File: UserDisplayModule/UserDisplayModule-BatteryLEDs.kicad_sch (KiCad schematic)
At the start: 17 parts, among them U5 74HC595

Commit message: doubled LEDs + started PCB
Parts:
- removed D10: BAT3, symbol Device:LED
- removed D5: BAT8, symbol Device:LED
- removed D6: BAT7, symbol Device:LED
- removed D7: BAT6, symbol Device:LED
- removed D8: BAT5, symbol Device:LED
- removed D9: BAT4, symbol Device:LED
- added D13: BAT7, LED_SMD:LED_0805_2012Metric, symbol Device:LED
- added D14, D16, D18, D20, D22, D24, D25, D26: BAT1, LED_SMD:LED_0805_2012Metric, symbol Device:LED
- added D15: BAT6, LED_SMD:LED_0805_2012Metric, symbol Device:LED
- added D17: BAT5, LED_SMD:LED_0805_2012Metric, symbol Device:LED
- added D19: BAT4, LED_SMD:LED_0805_2012Metric, symbol Device:LED
- added D21: BAT3, LED_SMD:LED_0805_2012Metric, symbol Device:LED
- added D23: BAT2, LED_SMD:LED_0805_2012Metric, symbol Device:LED
- D11: value BAT2 -> BAT8; footprint (none) -> LED_SMD:LED_0805_2012Metric
- D12: footprint (none) -> LED_SMD:LED_0805_2012Metric
- R10, R11, R12, R5, R6, R7, R8, R9: footprint (none) -> Resistor_SMD:R_0805_2012Metric
- U5: footprint (none) -> ImportedFootprints:CD74HC595E
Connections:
- net GND: now also D14.1 (K), D16.1 (K), D18.1 (K), D20.1 (K), D22.1 (K), D24.1 (K), D26.1 (K); no longer D11.1 (K)
- net at R10.2: now also D21.2 (A)
- net at R6.2: now also D13.2 (A)
- net at R5.2: now also D11.2 (A)
- net at R7.2: now also D15.2 (A)
- net at R9.2: now also D19.2 (A)
- net at R8.2: now also D17.2 (A)
- net at D12.2 (A): now also D11.1 (K); no longer R12.2
- net at R11.2: now also D23.2 (A); no longer D11.2 (A)
- new net: D21.1 (K), D22.2 (A)
- new net: D13.1 (K), D14.2 (A)
- new net: D25.1 (K), D26.2 (A)
- new net: D19.1 (K), D20.2 (A)
- new net: D17.1 (K), D18.2 (A)
- new net: D23.1 (K), D24.2 (A)
- new net: D15.1 (K), D16.2 (A)
- new net: D25.2 (A), R12.2
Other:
- note added: "Battery Bar"

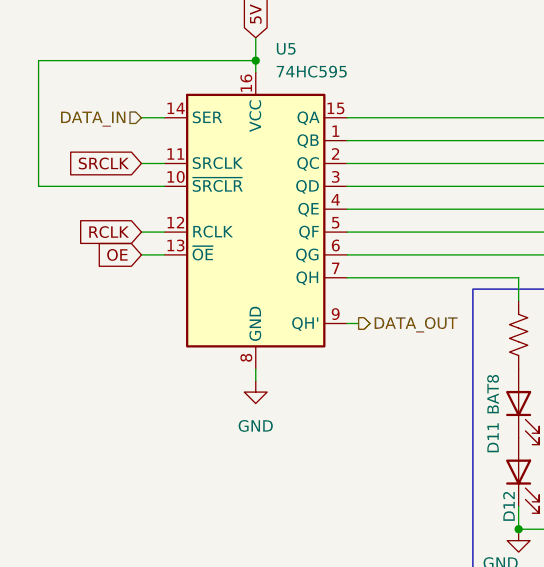
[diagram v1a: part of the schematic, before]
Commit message: finished routing pcb (minus ground pour)
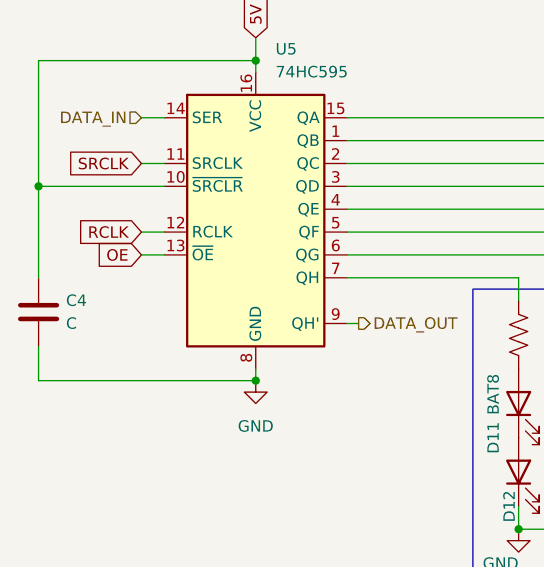
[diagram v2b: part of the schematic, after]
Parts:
- added C4: C, Capacitor_SMD:C_0805_2012Metric, symbol Device:C
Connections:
- net 5V: now also C4.1
- net GND: now also C4.2
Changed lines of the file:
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@@
+	)
+	(junction
+		(at 93.98 55.88)
+		(diameter 0)
+		(color 0 0 0 0)
 	)
 	(junction
@@
 		(color 0 0 0 0)
 	)
+	(junction
+		(at 118.11 77.47)
+		(diameter 0)
+		(color 0 0 0 0)
+	)
 	(wire
 		(pts
@@
 	(wire
 		(pts
+			(xy 93.98 77.47) (xy 118.11 77.47)
+		)
+		(stroke
+			(width 0)
+			(type default)
+		)
+	)
+	(wire
+		(pts
 			(xy 105.41 48.26) (xy 107.95 48.26)
 		)
@@
 	(wire
 		(pts
+			(xy 93.98 73.66) (xy 93.98 77.47)
+		)
+		(stroke
+			(width 0)
+			(type default)
+		)
+	)
+	(wire
+		(pts
 			(xy 175.26 93.98) (xy 189.23 93.98)
 		)
@@
 		(pts
 			(xy 217.17 93.98) (xy 231.14 93.98)
+		)
+		(stroke
+			(width 0)
+			(type default)
+		)
+	)
+	(wire
+		(pts
+			(xy 93.98 55.88) (xy 93.98 66.04)
 		)
 		(stroke
@@
 					(unit 1)
 				)
+			)
+		)
+	)
+	(symbol
+		(lib_id "Device:C")
+		(at 93.98 69.85 0)
+		(unit 1)
+		(exclude_from_sim no)
+		(in_bom yes)
+		(on_board yes)
+		(dnp no)
+		(property "Reference" "C4"
+			(at 97.028 68.58 0)
+			(effects
+				(font
+					(size 1.27 1.27)
+				)
+				(justify left)
+			)
+		)
+		(property "Value" "C"
+			(at 97.028 71.12 0)
+			(effects
+				(font
+					(size 1.27 1.27)
+				)
+				(justify left)
+			)
+		)
+		(property "Footprint" "Capacitor_SMD:C_0805_2012Metric"
+			(at 94.9452 73.66 0)
+			(effects
+				(font
+					(size 1.27 1.27)
+				)
+				(hide yes)
+			)
+		)
+		(property "Datasheet" "~"
+			(at 93.98 69.85 0)
+			(effects
+				(font
+					(size 1.27 1.27)
+				)
+				(hide yes)
+			)
+		)
+		(property "Description" "Unpolarized capacitor"
+			(at 93.98 69.85 0)
+			(effects
+				(font
+					(size 1.27 1.27)
+				)
+				(hide yes)
+			)
+		)
+		(pin "2"
+		)
+		(pin "1"
+		)
+		(instances
+			(project "UserDisplayModule"
+				(path "/352d7abe-fc72-4473-8b68-62eecf44f496/4dda0760-e028-41e6-8bb4-4ea7d454afd7"
+					(reference "C4")
+					(unit 1)
+				)

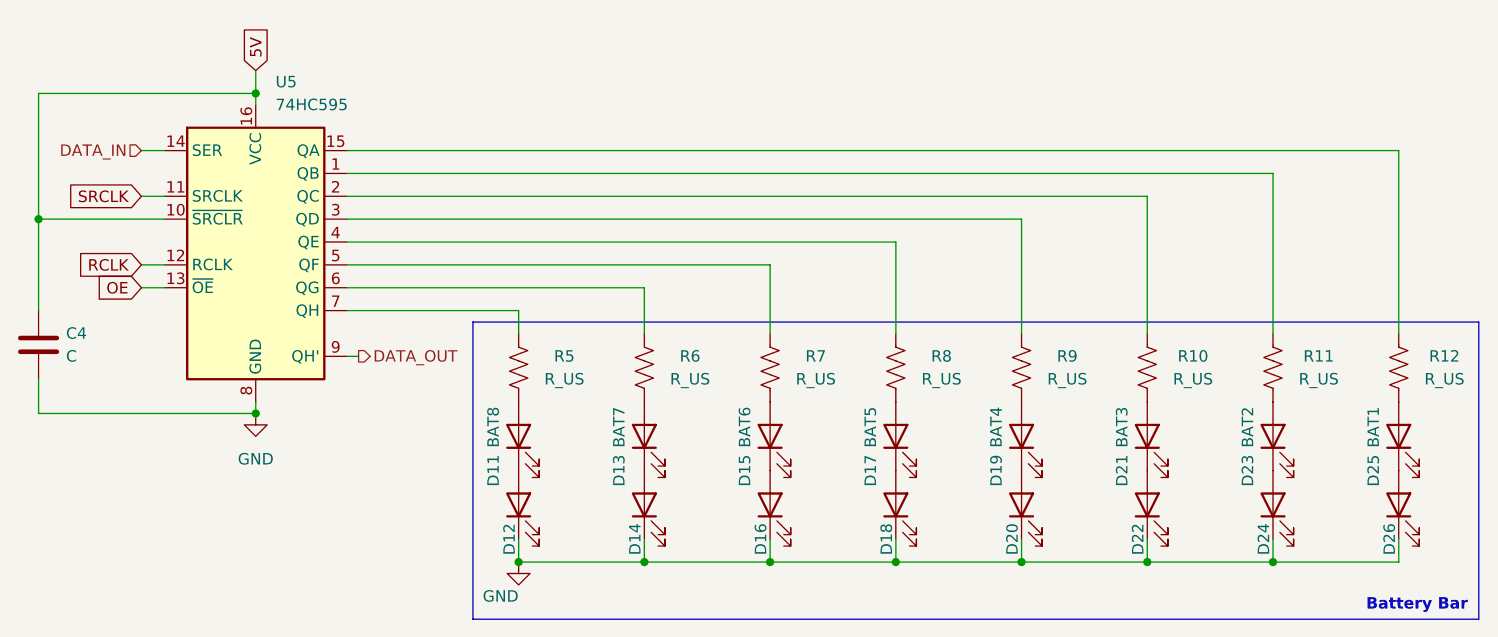
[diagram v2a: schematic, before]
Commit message: added 3d models, fixed footprints, finished routing
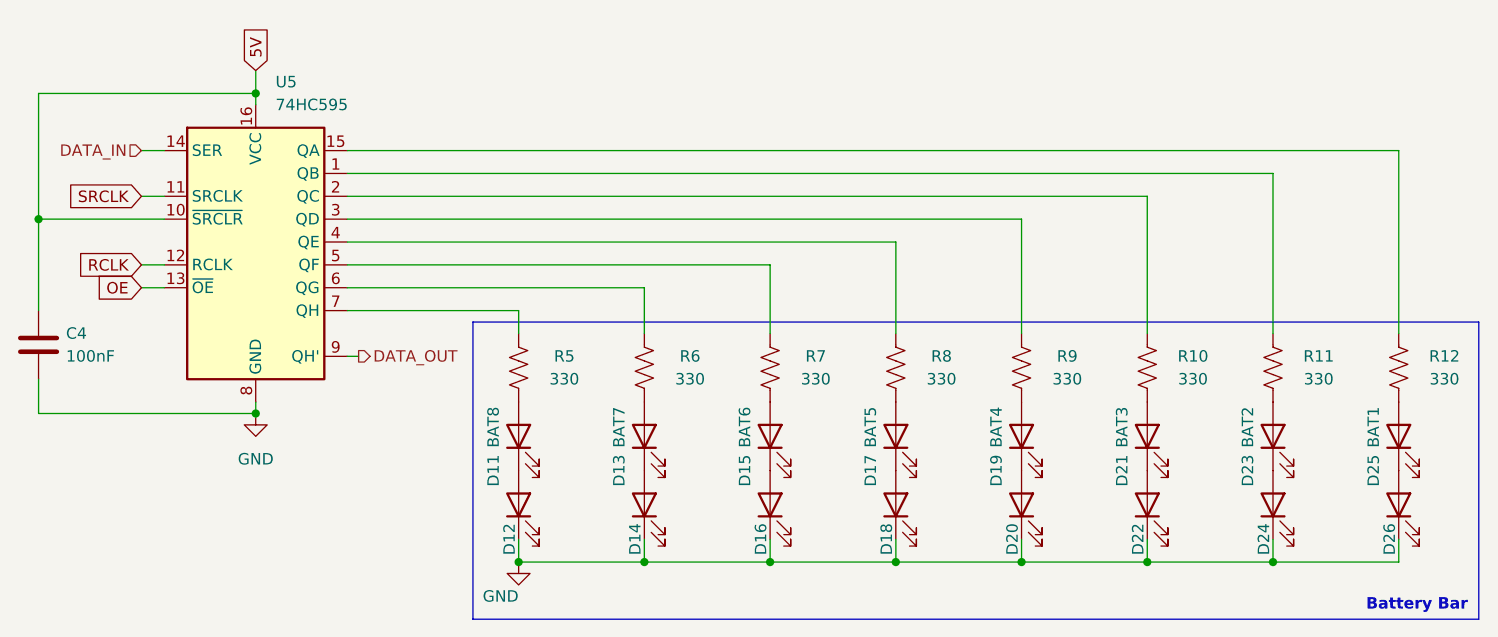
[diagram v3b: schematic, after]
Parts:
- C4: value C -> 100nF
- R10, R11, R12, R5, R6, R7, R8, R9: value R_US -> 330
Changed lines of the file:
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@@
 			)
 		)
-		(property "Value" "R_US"
+		(property "Value" "330"
 			(at 222.25 73.66 0)
 			(effects
@@
 			)
 		)
-		(property "Value" "R_US"
+		(property "Value" "330"
 			(at 166.37 73.66 0)
 			(effects
@@
 			)
 		)
-		(property "Value" "R_US"
+		(property "Value" "330"
 			(at 180.34 73.66 0)
 			(effects
@@
 			)
 		)
-		(property "Value" "C"
+		(property "Value" "100nF"
 			(at 97.028 71.12 0)
 			(effects
@@
 			)
 		)
-		(property "Value" "R_US"
+		(property "Value" "330"
 			(at 194.31 73.66 0)
 			(effects
@@
 			)
 		)
-		(property "Value" "R_US"
+		(property "Value" "330"
 			(at 208.28 73.66 0)
 			(effects
@@
 			)
 		)
-		(property "Value" "R_US"
+		(property "Value" "330"
 			(at 152.4 73.66 0)
 			(effects
@@
 			)
 		)
-		(property "Value" "R_US"
+		(property "Value" "330"
 			(at 236.22 73.66 0)
 			(effects
@@
 			)
 		)
-		(property "Value" "R_US"
+		(property "Value" "330"
 			(at 250.19 73.66 0)
 			(effects

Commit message: added digikey pns
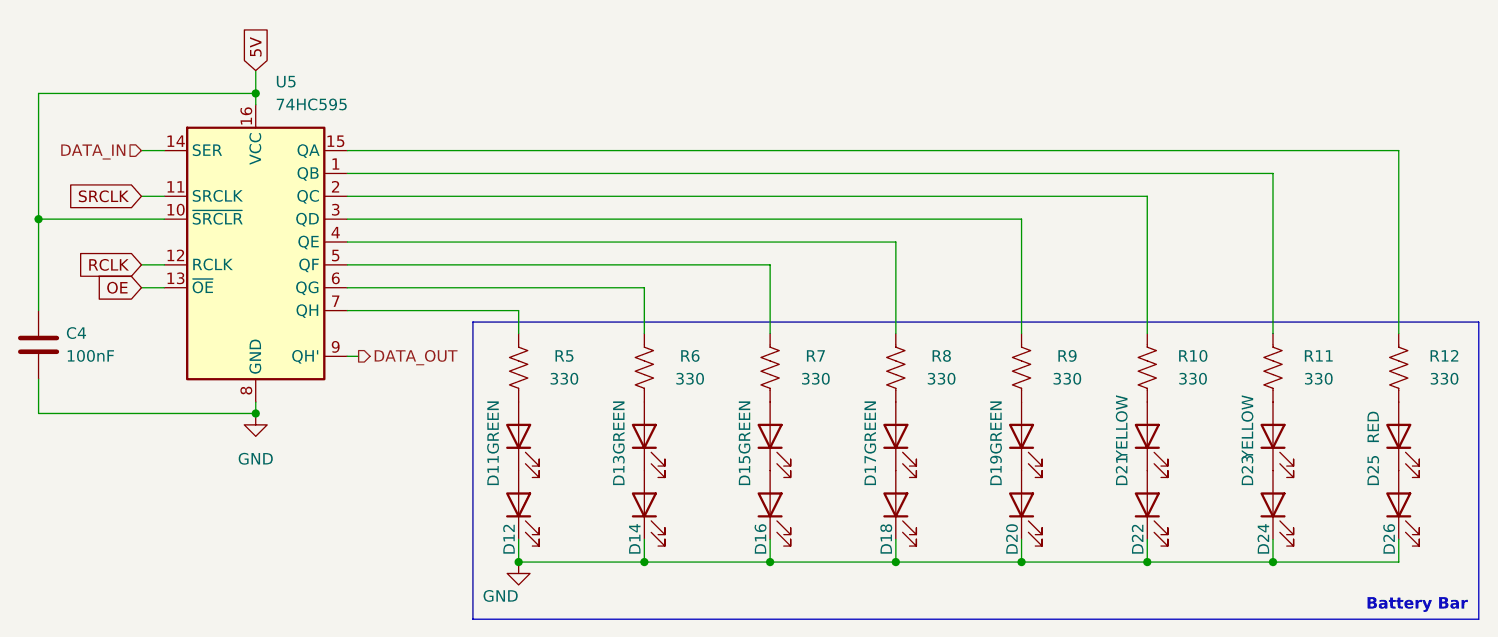
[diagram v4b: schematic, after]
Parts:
- D11: value BAT8 -> GREEN; Digikey PN (none) -> 732-4983-1-ND
- D12, D14, D16, D18, D20: value BAT1 -> GREEN; Digikey PN (none) -> 732-4983-1-ND
- D13: value BAT7 -> GREEN; Digikey PN (none) -> 732-4983-1-ND
- D15: value BAT6 -> GREEN; Digikey PN (none) -> 732-4983-1-ND
- D17: value BAT5 -> GREEN; Digikey PN (none) -> 732-4983-1-ND
- D19: value BAT4 -> GREEN; Digikey PN (none) -> 732-4983-1-ND
- D21: value BAT3 -> YELLOW; Digikey PN (none) -> 732-4987-1-ND
- D22, D24: value BAT1 -> YELLOW; Digikey PN (none) -> 732-4987-1-ND
- D23: value BAT2 -> YELLOW; Digikey PN (none) -> 732-4987-1-ND
- D25, D26: value BAT1 -> RED; Digikey PN (none) -> 732-4984-1-ND
- U5: Digikey PN (none) -> 296-1600-5-ND

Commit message: Edited BOM for R/C parts
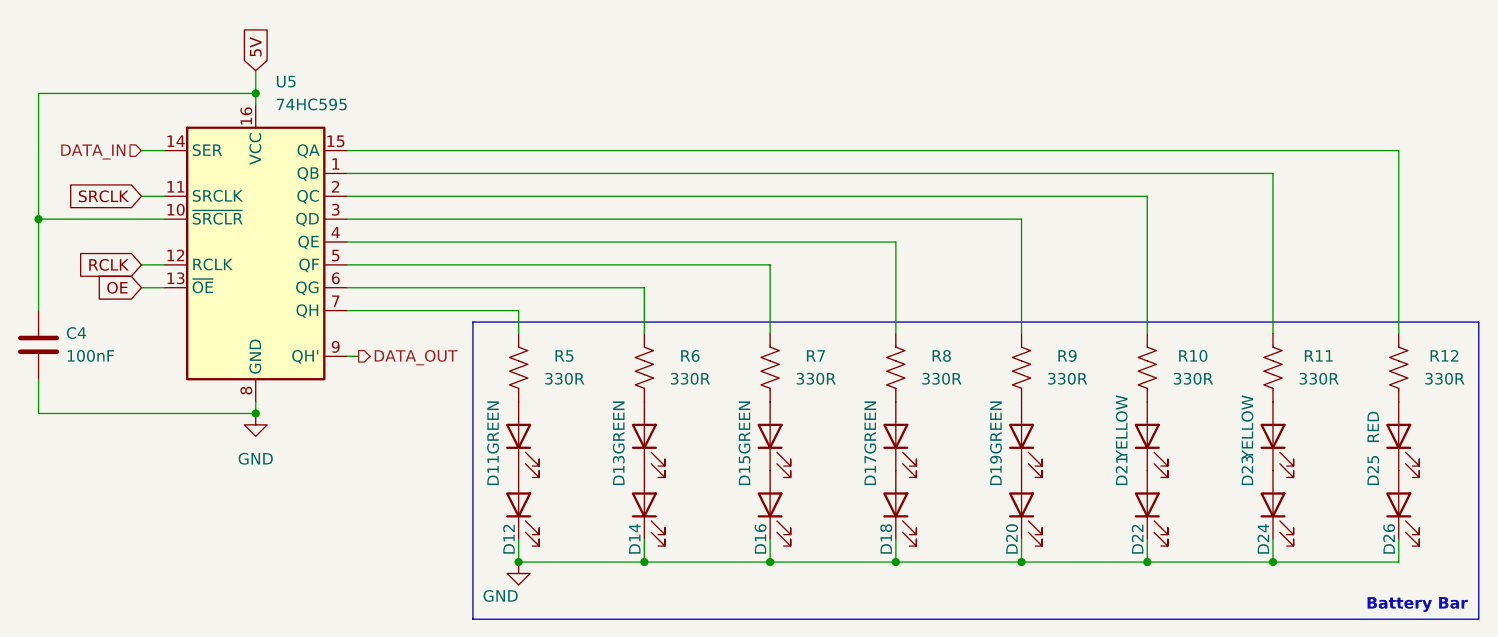
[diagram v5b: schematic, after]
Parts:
- C4: Digikey PN (none) -> 1276-1003-1-ND
- R10, R11, R12, R5, R6, R7, R8, R9: value 330 -> 330R; Digikey PN (none) -> RMCF0805FT330RCT-ND
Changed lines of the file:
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@@
 			)
 		)
-		(property "Value" "330"
+		(property "Value" "330R"
 			(at 222.25 73.66 0)
 			(effects
@@
 			)
 		)
-		(property "Digikey PN" ""
+		(property "Digikey PN" "RMCF0805FT330RCT-ND"
 			(at 217.17 72.39 0)
 			(effects
@@
 			)
 		)
-		(property "Value" "330"
+		(property "Value" "330R"
 			(at 166.37 73.66 0)
 			(effects
@@
 			)
 		)
-		(property "Digikey PN" ""
+		(property "Digikey PN" "RMCF0805FT330RCT-ND"
 			(at 161.29 72.39 0)
 			(effects
@@
 			)
 		)
-		(property "Value" "330"
+		(property "Value" "330R"
 			(at 180.34 73.66 0)
 			(effects
@@
 			)
 		)
-		(property "Digikey PN" ""
+		(property "Digikey PN" "RMCF0805FT330RCT-ND"
 			(at 175.26 72.39 0)
 			(effects
@@
 			)
 		)
-		(property "Digikey PN" ""
+		(property "Digikey PN" "1276-1003-1-ND"
 			(at 93.98 69.85 0)
 			(effects
@@
 			)
 		)
-		(property "Value" "330"
+		(property "Value" "330R"
 			(at 194.31 73.66 0)
 			(effects
@@
 			)
 		)
-		(property "Digikey PN" ""
+		(property "Digikey PN" "RMCF0805FT330RCT-ND"
 			(at 189.23 72.39 0)
 			(effects
@@
 			)
 		)
-		(property "Value" "330"
+		(property "Value" "330R"
 			(at 208.28 73.66 0)
 			(effects
@@
 			)
 		)
-		(property "Digikey PN" ""
+		(property "Digikey PN" "RMCF0805FT330RCT-ND"
 			(at 203.2 72.39 0)
 			(effects
@@
 			)
 		)
-		(property "Value" "330"
+		(property "Value" "330R"
 			(at 152.4 73.66 0)
 			(effects
@@
 			)
 		)
-		(property "Digikey PN" ""
+		(property "Digikey PN" "RMCF0805FT330RCT-ND"
 			(at 147.32 72.39 0)
 			(effects
@@
 			)
 		)
-		(property "Value" "330"
+		(property "Value" "330R"
 			(at 236.22 73.66 0)
 			(effects
@@
 			)
 		)
-		(property "Digikey PN" ""
+		(property "Digikey PN" "RMCF0805FT330RCT-ND"
 			(at 231.14 72.39 0)
 			(effects
@@
 			)
 		)
-		(property "Value" "330"
+		(property "Value" "330R"
 			(at 250.19 73.66 0)
 			(effects
@@
 			)
 		)
-		(property "Digikey PN" ""
+		(property "Digikey PN" "RMCF0805FT330RCT-ND"
 			(at 245.11 72.39 0)
 			(effects
